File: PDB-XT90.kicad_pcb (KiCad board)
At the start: 2 copper layers, 50 x 50 mm, 10 parts

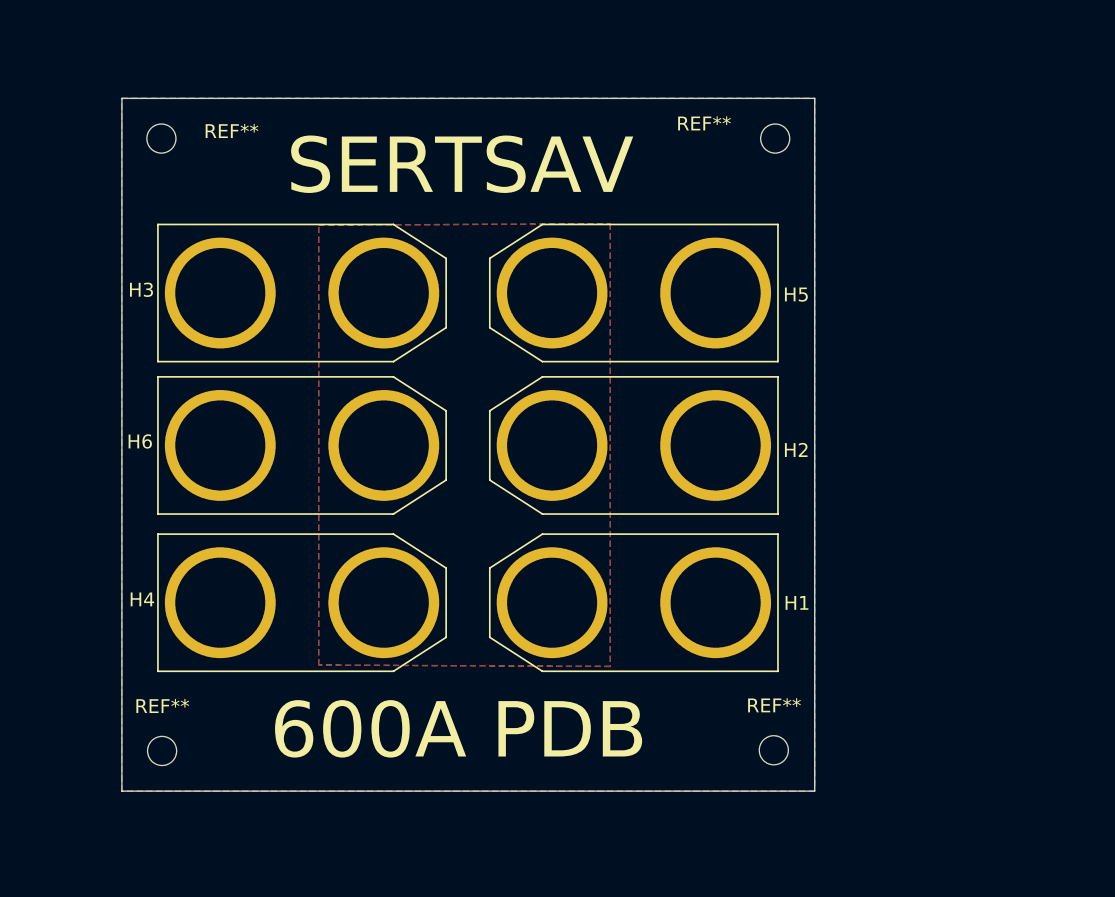
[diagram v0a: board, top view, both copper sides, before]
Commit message: Added logos
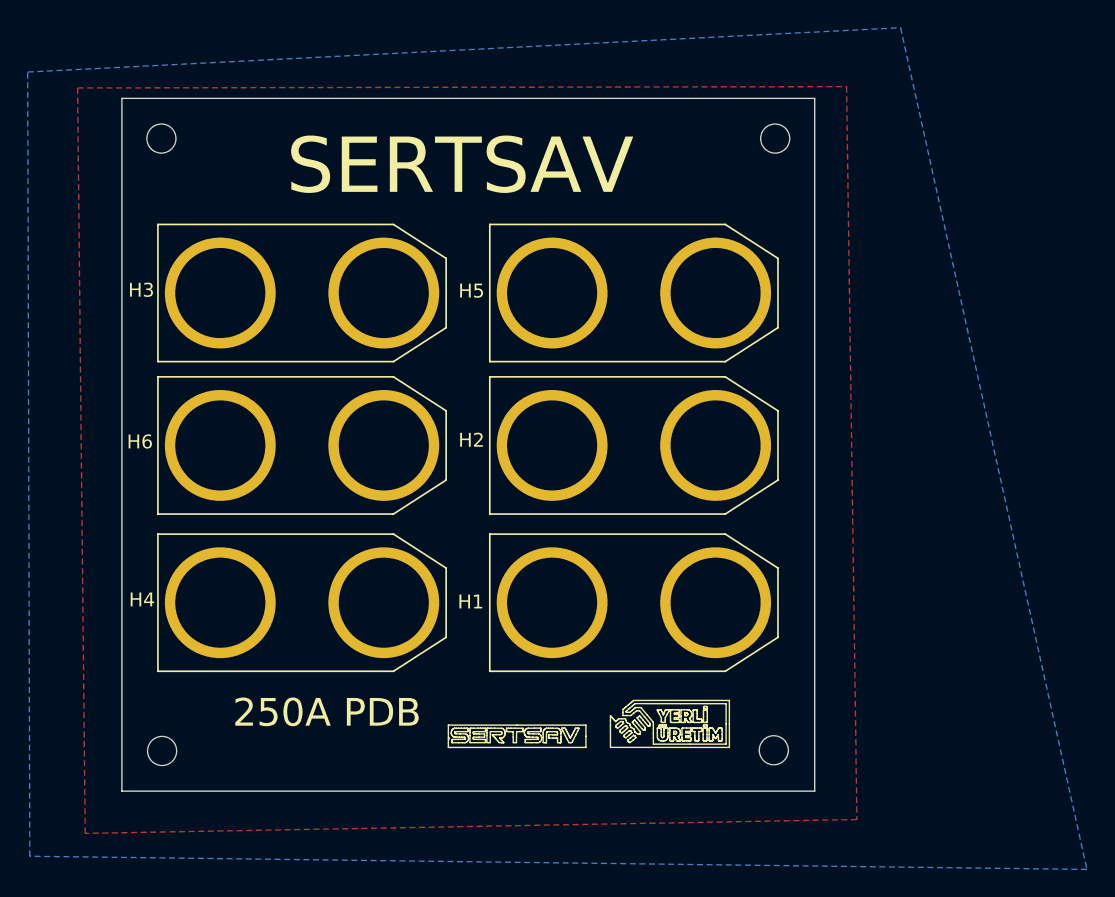
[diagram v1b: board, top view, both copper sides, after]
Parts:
- turned H1 to 0 degrees
- turned H2 to 0 degrees
- turned H5 to 0 degrees
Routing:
- removed copper zone on F.Cu, net GND
- removed copper zone on B.Cu, net VCC
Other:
- board text added: "250A PDB"
- board text removed: "600A PDB"
